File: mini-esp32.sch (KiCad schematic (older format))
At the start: 47 parts, among them J1 BAT, J2 USB_B_Micro, J5 Conn_01x18, J6 Conn_01x18, Q1 AO3401A, Q2 S8050, Q3 S8050, SW1 RESET, U1 ESP32-WROOM-32E, U2 RT9080-33GJ5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

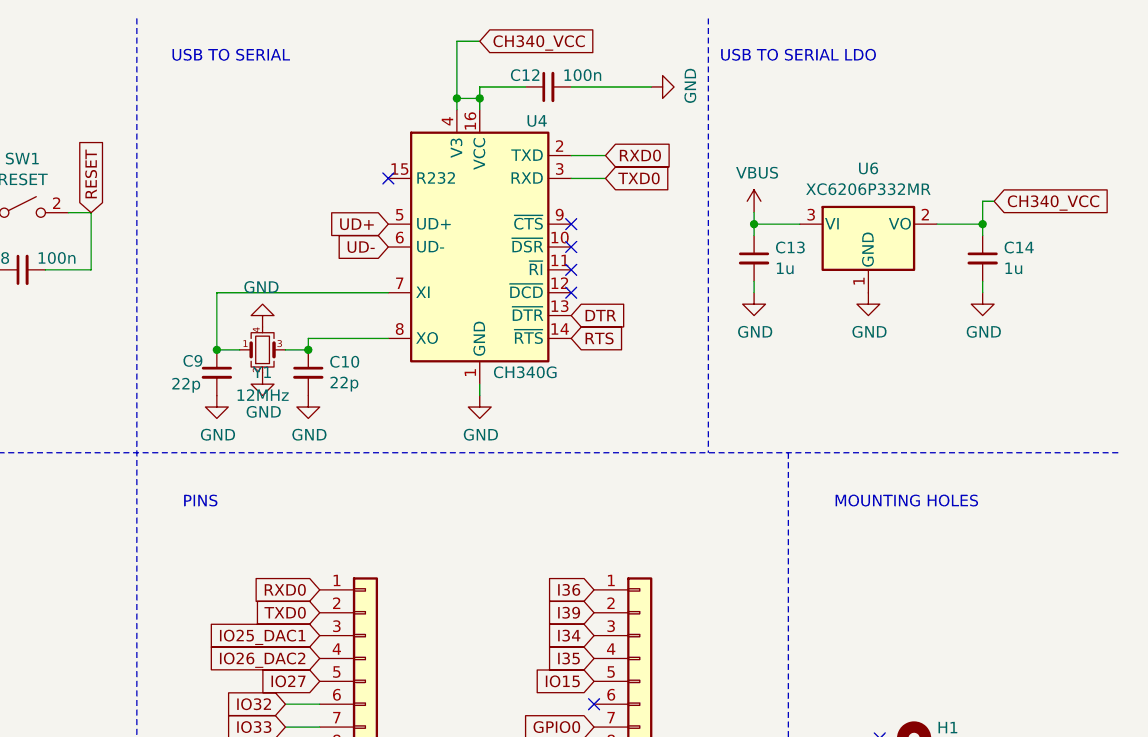
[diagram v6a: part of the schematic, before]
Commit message: Change USB-to-Serial to CP2104
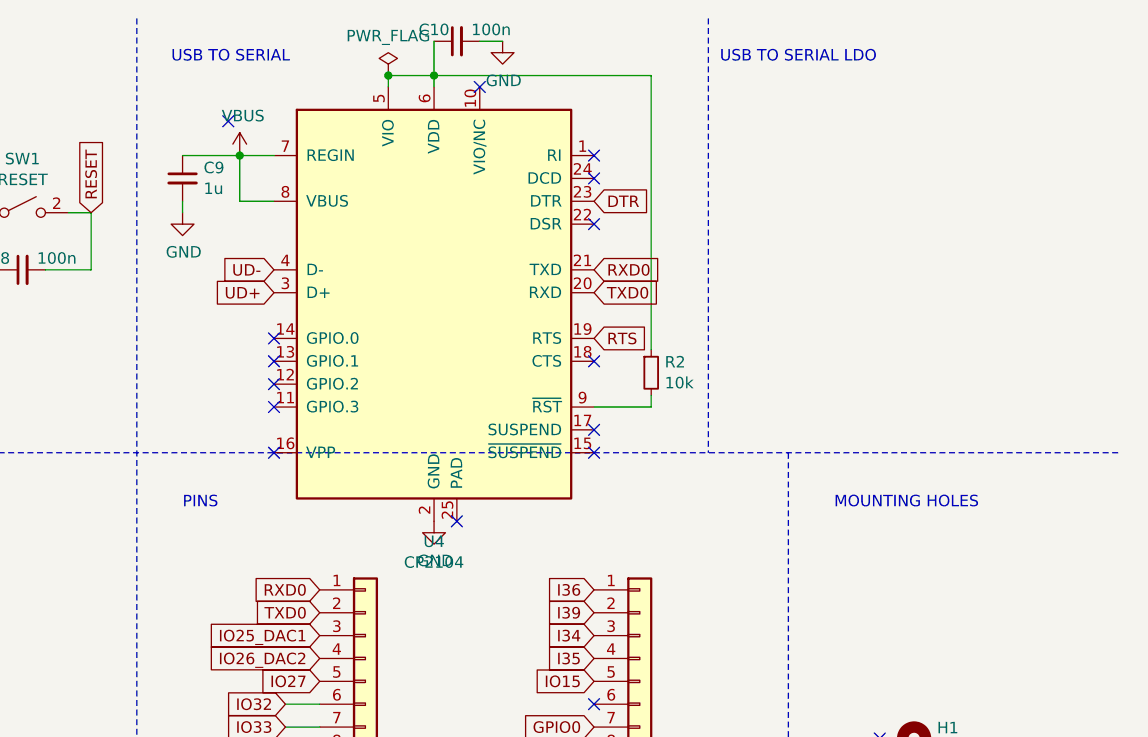
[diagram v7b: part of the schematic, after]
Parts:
- removed C12: 100n, Capacitor_SMD:C_0402_1005Metric, symbol Device:C_Small
- removed C13, C14: 1u, Capacitor_SMD:C_0402_1005Metric, symbol Device:C_Small
- removed U4: CH340G, Package_SO:SOIC-16_3.9x9.9mm_P1.27mm, symbol Interface_USB:CH340G
- removed U6: XC6206P332MR, Package_TO_SOT_SMD:SOT-23, symbol Regulator_Linear:XC6206PxxxMR
- removed Y1: 12MHz, Crystal:Crystal_SMD_3225-4Pin_3.2x2.5mm, symbol Device:Crystal_GND24_Small
- added R2: 10k, Resistor_SMD:R_0402_1005Metric, symbol Device:R_Small
- added U4: CP2104, Package_DFN_QFN:QFN-24-1EP_4x4mm_P0.5mm_EP2.6x2.6mm, symbol Interface_USB:CP2104
- C10: value 22p -> 100n; LCSC Part # C1555 -> C1525
- C9: value 22p -> 1u; LCSC Part # C1555 -> C52923
- U1: LCSC Part # C701343 -> C701341
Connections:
- net DTR: now also U4.23 (DTR)
- net GND: now also U4.2 (GND)
- net RTS: now also U4.19 (RTS)
- net RXD0: now also U4.21 (TXD)
- net TXD0: now also U4.20 (RXD)
- net UD+: now also U4.3 (D+)
- net UD-: now also U4.4 (D-)
- net VBUS: now also C9.1, U4.7 (REGIN), U4.8 (VBUS)
- net at C10.1: now also R2.1, U4.5 (VIO), U4.6 (VDD)
- new net: R2.2, U4.9 (~RST)
- no-connect marks 22 -> 31
